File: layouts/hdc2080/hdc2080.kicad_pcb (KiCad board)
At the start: 2 copper layers, 2 parts

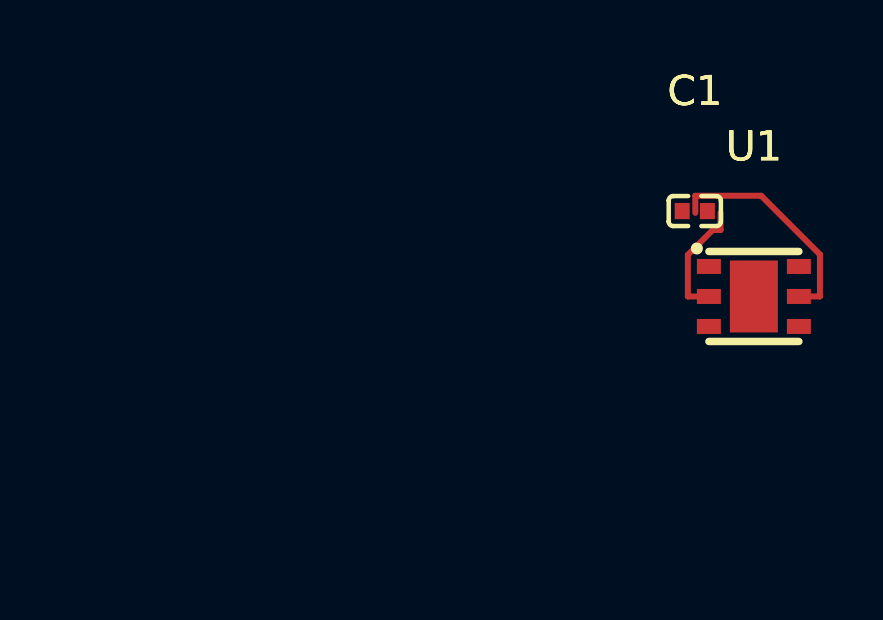
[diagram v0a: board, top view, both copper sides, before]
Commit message: Enhance smart placer with simulated annealing and pre-routing validation
Smart Placer improvements:
- Add simulated annealing refinement (now default) for better wire length optimization
- Add force-directed refinement with improvement safeguard
- Add silkscreen text repositioning to avoid component overlaps
- Significant wire length reductions (e.g., power_filter: 113mm -> 46mm)

Autorouter improvements:
- Add PreRoutingValidator class for pre-flight checks
- Validate unconnected pads, overlapping footprints, unplaced components
- Use pad-based bounds for accurate overlap detection
- Block routing on validation errors with actionable messages

Research:
- Add comprehensive autorouting/autoplacement findings document
- Cover Freerouting Python client, OrthoRoute, DeepPCB, KiCad 9 IPC API
- Document force-directed and simulated annealing algorithms

Cleanup:
- Update .gitignore for DSN/SES files, build artifacts, tools
- Remove stale timestamped build files
- Add parts footprints and symbols

All 10 modules placed and routed successfully.

Co-Authored-By: Claude Opus 4.5 <noreply@anthropic.com>
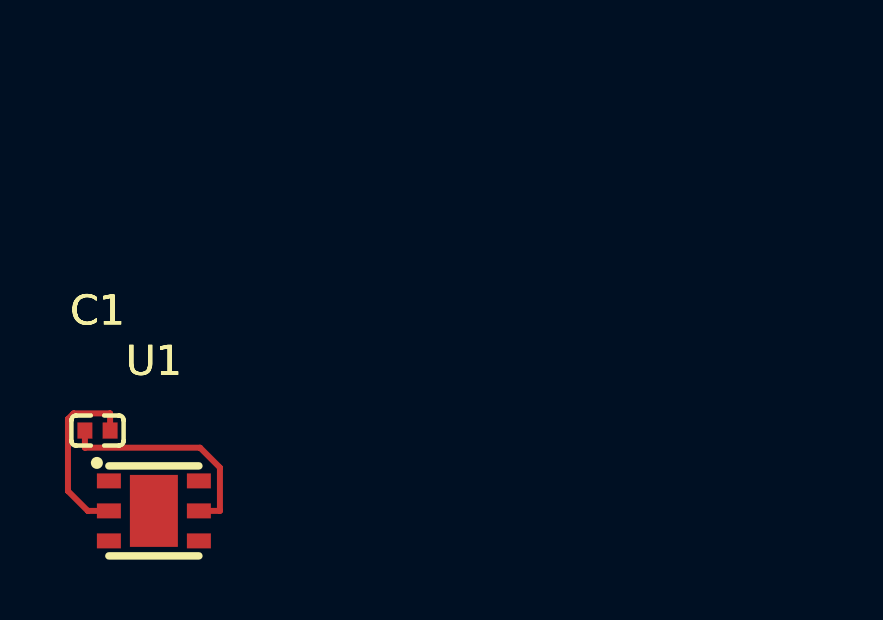
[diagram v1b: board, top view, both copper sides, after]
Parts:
- moved U1 21.2 mm to (80.0, 107.1)
- moved C1 21.2 mm to (78.1, 104.5)
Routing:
- net gnd: track 4.09 -> 6.09 mm
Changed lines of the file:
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@@
 	(footprint "Texas_Instruments_HDC2080DMBR:WSON-6_L3.0-W3.0-P1.00-TL-EP"
 		(layer "F.Cu")
-		(at 100 100)
+		(at 80 107.1475)
 		(property "Reference" "U1"
 			(at 0 -5 0)
@@
 	(footprint "Samsung_Electro_Mechanics_CL05B104KO5NNNC:C0402"
 		(layer "F.Cu")
-		(at 98.030384 97.152703)
+		(at 78.1206 104.4689)
 		(property "Reference" "C1"
 			(at 0 -4 0)
@@
 	)
 	(segment
-		(start 97.7983 98.6141)
-		(end 98.6263 97.7861)
+		(start 77.1362 106.4854)
+		(end 77.7983 107.1475)
 		(width 0.2)
 		(layer "F.Cu")
@@
 	)
 	(segment
-		(start 97.7983 100)
-		(end 97.7983 98.6141)
+		(start 77.3237 103.8972)
+		(end 77.1362 104.0847)
 		(width 0.2)
 		(layer "F.Cu")
@@
 	)
 	(segment
-		(start 98.6263 97.7861)
-		(end 98.8879 97.7861)
+		(start 78.5406 104.4689)
+		(end 78.5406 103.8972)
 		(width 0.2)
 		(layer "F.Cu")
@@
 	)
 	(segment
-		(start 98.8879 97.2144)
-		(end 98.8879 97.7861)
+		(start 78.5406 103.8972)
+		(end 77.3237 103.8972)
 		(width 0.2)
 		(layer "F.Cu")
@@
 	)
 	(segment
-		(start 98.5 100)
-		(end 97.7983 100)
+		(start 77.1362 104.0847)
+		(end 77.1362 106.4854)
 		(width 0.2)
 		(layer "F.Cu")
@@
 	)
 	(segment
-		(start 102.2017 98.6)
-		(end 100.2444 96.6427)
+		(start 78.5 107.1475)
+		(end 77.7983 107.1475)
+		(width 0.2)
+		(layer "F.Cu")
+		(net 3)
+	)
+	(segment
+		(start 77.7006 104.4689)
+		(end 77.7006 105.0406)
 		(width 0.2)
 		(layer "F.Cu")
@@
 	)
 	(segment
-		(start 98.0479 97.2144)
-		(end 98.0479 96.6427)
+		(start 81.5 107.1475)
+		(end 82.2017 107.1475)
 		(width 0.2)
 		(layer "F.Cu")
@@
 	)
 	(segment
-		(start 100.2444 96.6427)
-		(end 98.0479 96.6427)
+		(start 82.2017 107.1475)
+		(end 82.2017 105.7042)
 		(width 0.2)
 		(layer "F.Cu")
@@
 	)
 	(segment
-		(start 102.2017 100)
-		(end 102.2017 98.6)
+		(start 81.5381 105.0406)
+		(end 77.7006 105.0406)
 		(width 0.2)
 		(layer "F.Cu")
@@
 	)
 	(segment
-		(start 101.5 100)
-		(end 102.2017 100)
-		(width 0.2)
-		(layer "F.Cu")
+		(start 82.2017 105.7042)
+		(end 81.5381 105.0406)
+		(width 0.2)
+		(layer "F.Cu")
